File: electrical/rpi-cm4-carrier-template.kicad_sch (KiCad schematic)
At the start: 0 parts

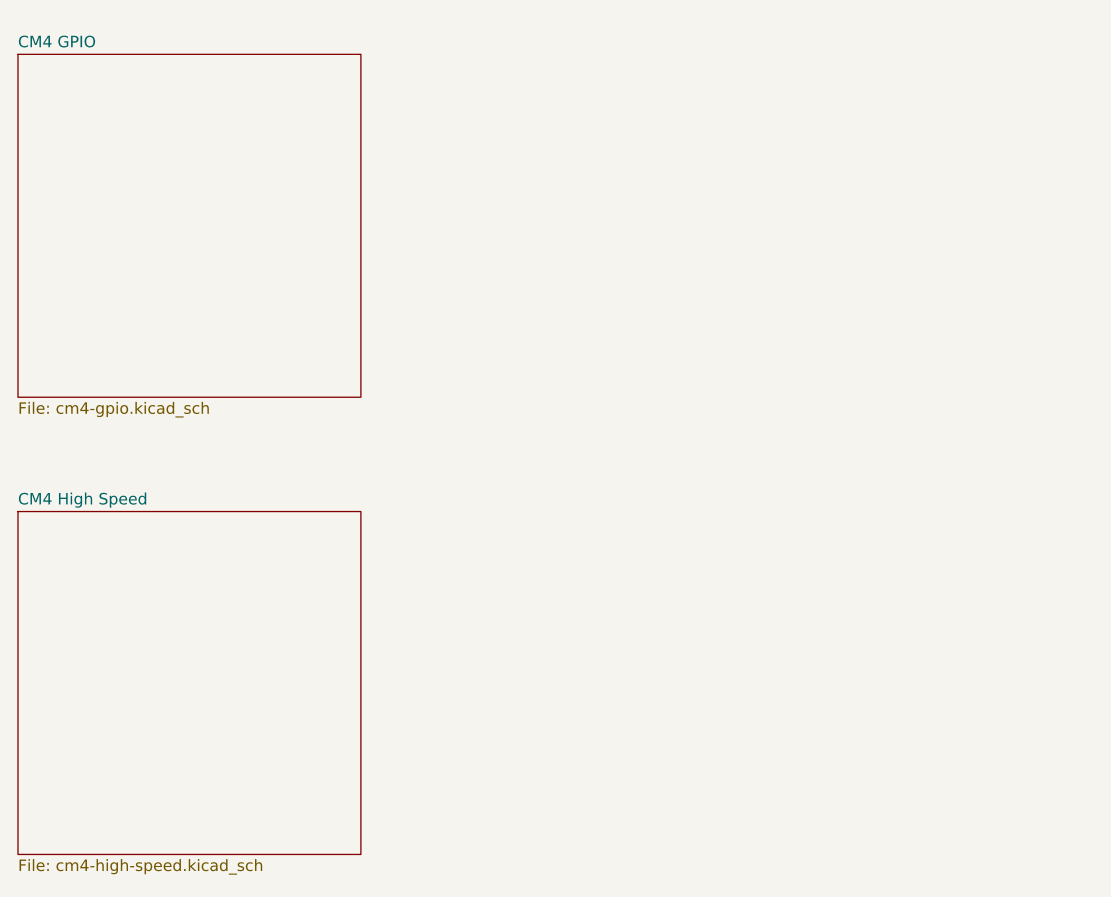
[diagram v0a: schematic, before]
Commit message: RJ-45 <-> KSZ9897R schematic connections
Also switched to a different RJ-45 port: Belfuse 0826-1G1T-23-F
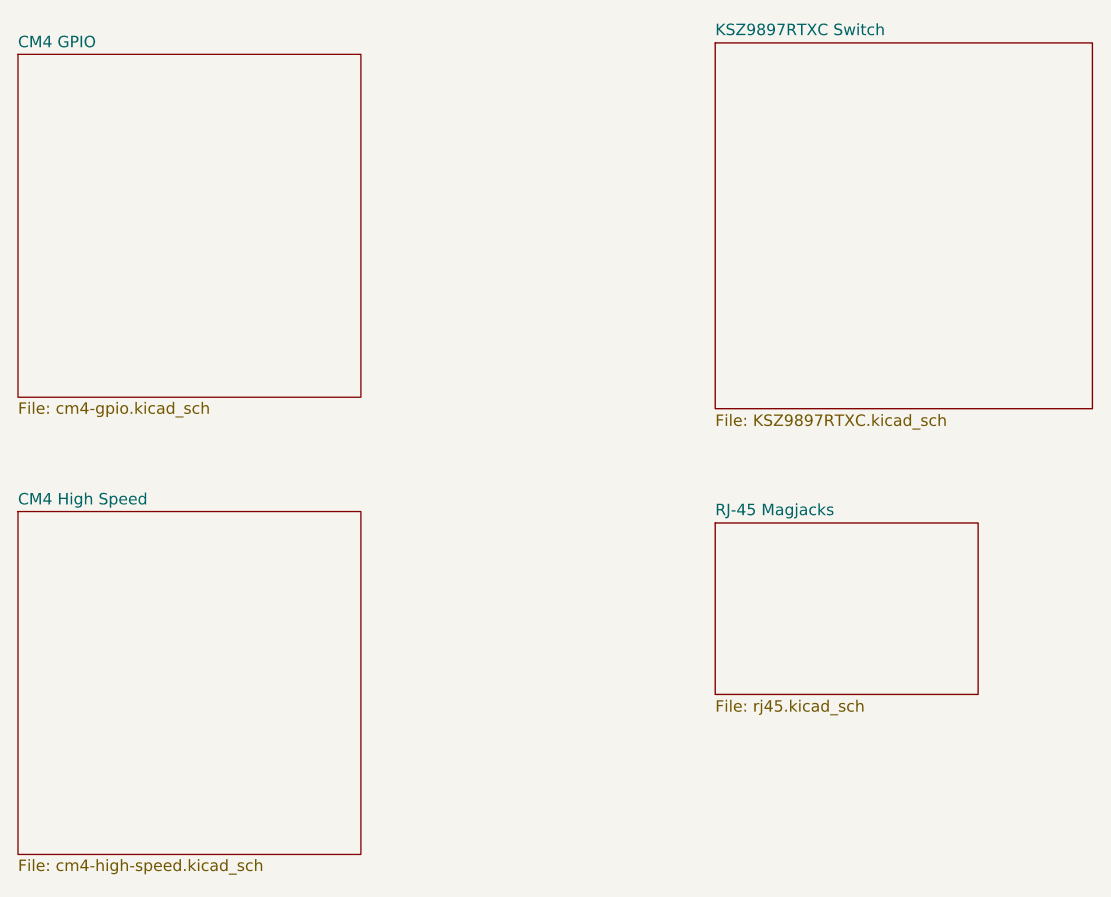
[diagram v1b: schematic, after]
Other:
- added sheet KSZ9897RTXC Switch (KSZ9897RTXC.kicad_sch)
- added sheet RJ-45 Magjacks (rj45.kicad_sch)
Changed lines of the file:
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@@
+	)
+	(sheet
+		(at 179.07 102.87)
+		(size 29.21 19.05)
+		(fields_autoplaced yes)
+		(stroke
+			(width 0.1524)
+			(type solid)
+		)
+		(fill
+			(color 0 0 0 0.0000)
+		)
+		(property "Sheetname" "RJ-45 Magjacks"
+			(at 179.07 102.1584 0)
+			(effects
+				(font
+					(size 1.27 1.27)
+				)
+				(justify left bottom)
+			)
+		)
+		(property "Sheetfile" "rj45.kicad_sch"
+			(at 179.07 122.5046 0)
+			(effects
+				(font
+					(size 1.27 1.27)
+				)
+				(justify left top)
+			)
+		)
+		(instances
+			(project "rpi-cm4-carrier-template"
+				(path "/87b93ef3-3469-436c-9ae8-16e6c9607244"
+					(page "5")
+				)
+			)
+		)
+	)
+	(sheet
+		(at 179.07 49.53)
+		(size 41.91 40.64)
+		(fields_autoplaced yes)
+		(stroke
+			(width 0.1524)
+			(type solid)
+		)
+		(fill
+			(color 0 0 0 0.0000)
+		)
+		(property "Sheetname" "KSZ9897RTXC Switch"
+			(at 179.07 48.8184 0)
+			(effects
+				(font
+					(size 1.27 1.27)
+				)
+				(justify left bottom)
+			)
+		)
+		(property "Sheetfile" "KSZ9897RTXC.kicad_sch"
+			(at 179.07 90.7546 0)
+			(effects
+				(font
+					(size 1.27 1.27)
+				)
+				(justify left top)
+			)
+		)
+		(instances
+			(project "rpi-cm4-carrier-template"
+				(path "/87b93ef3-3469-436c-9ae8-16e6c9607244"
+					(page "4")
+				)
+			)
+		)
 	)
 	(sheet

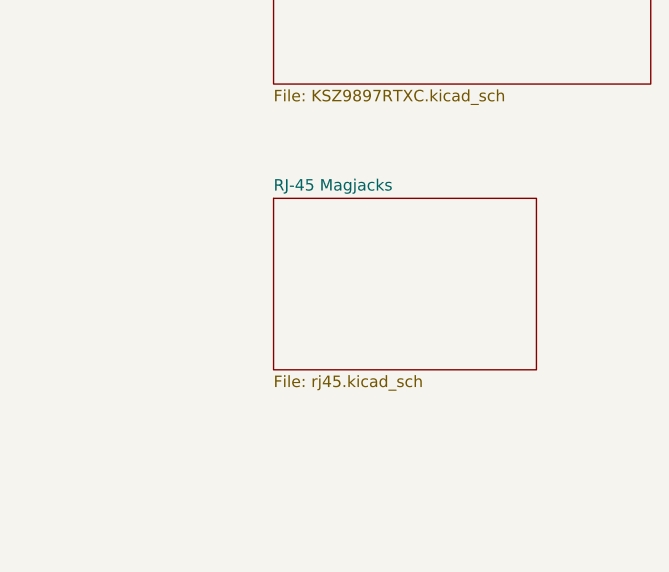
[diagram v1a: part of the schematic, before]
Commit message: 25MHz crystal for KSZ9897
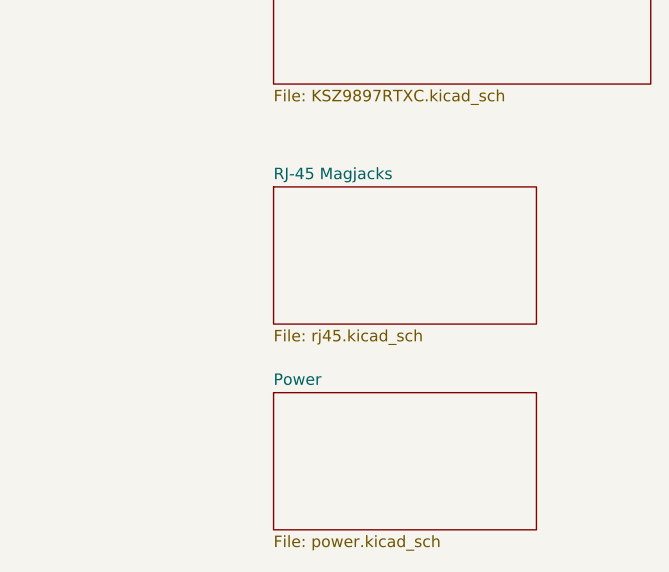
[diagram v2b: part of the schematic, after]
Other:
- added sheet Power (power.kicad_sch)
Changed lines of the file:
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@@
 	)
 	(sheet
-		(at 179.07 102.87)
-		(size 29.21 19.05)
+		(at 179.07 124.46)
+		(size 29.21 15.24)
+		(fields_autoplaced yes)
+		(stroke
+			(width 0.1524)
+			(type solid)
+		)
+		(fill
+			(color 0 0 0 0.0000)
+		)
+		(property "Sheetname" "Power"
+			(at 179.07 123.7484 0)
+			(effects
+				(font
+					(size 1.27 1.27)
+				)
+				(justify left bottom)
+			)
+		)
+		(property "Sheetfile" "power.kicad_sch"
+			(at 179.07 140.2846 0)
+			(effects
+				(font
+					(size 1.27 1.27)
+				)
+				(justify left top)
+			)
+		)
+		(instances
+			(project "rpi-cm4-carrier-template"
+				(path "/87b93ef3-3469-436c-9ae8-16e6c9607244"
+					(page "6")
+				)
+			)
+		)
+	)
+	(sheet
+		(at 179.07 101.6)
+		(size 29.21 15.24)
 		(fields_autoplaced yes)
 		(stroke
@@
 		)
 		(property "Sheetname" "RJ-45 Magjacks"
-			(at 179.07 102.1584 0)
+			(at 179.07 100.8884 0)
 			(effects
 				(font
@@
 		)
 		(property "Sheetfile" "rj45.kicad_sch"
-			(at 179.07 122.5046 0)
+			(at 179.07 117.4246 0)
 			(effects
 				(font

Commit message: Micro B + Header for eMMC flash
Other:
- title: Raspberry Pi Compute Module 4 Carrier Template -> Network Tap
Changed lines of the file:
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@@
 	(paper "A4")
 	(title_block
-		(title "Raspberry Pi Compute Module 4 Carrier Template")
+		(title "Network Tap")
 		(date "2020-10-31")
 		(rev "v01")
